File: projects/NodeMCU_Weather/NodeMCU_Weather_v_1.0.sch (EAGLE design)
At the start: 4 parts

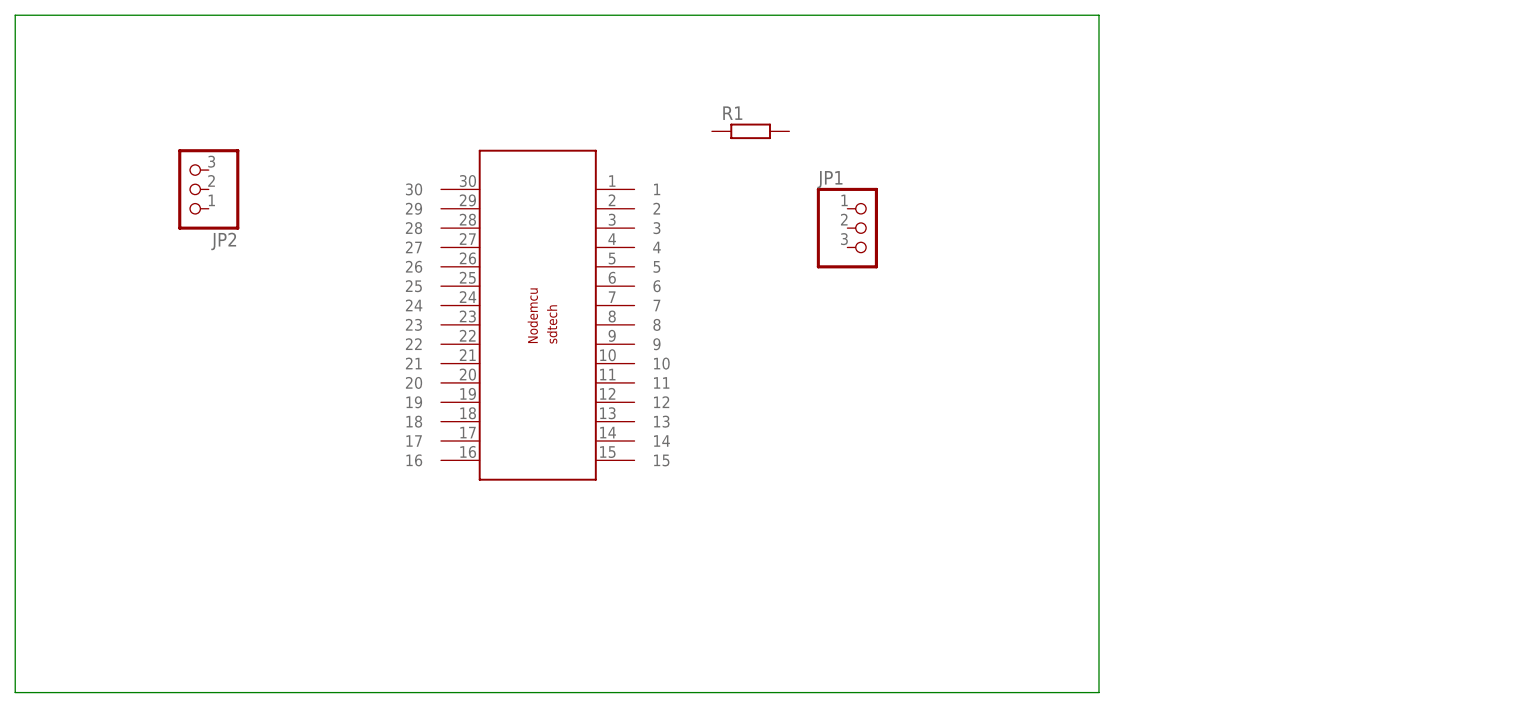
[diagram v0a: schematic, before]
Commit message: Base of nodemcu schematics and board
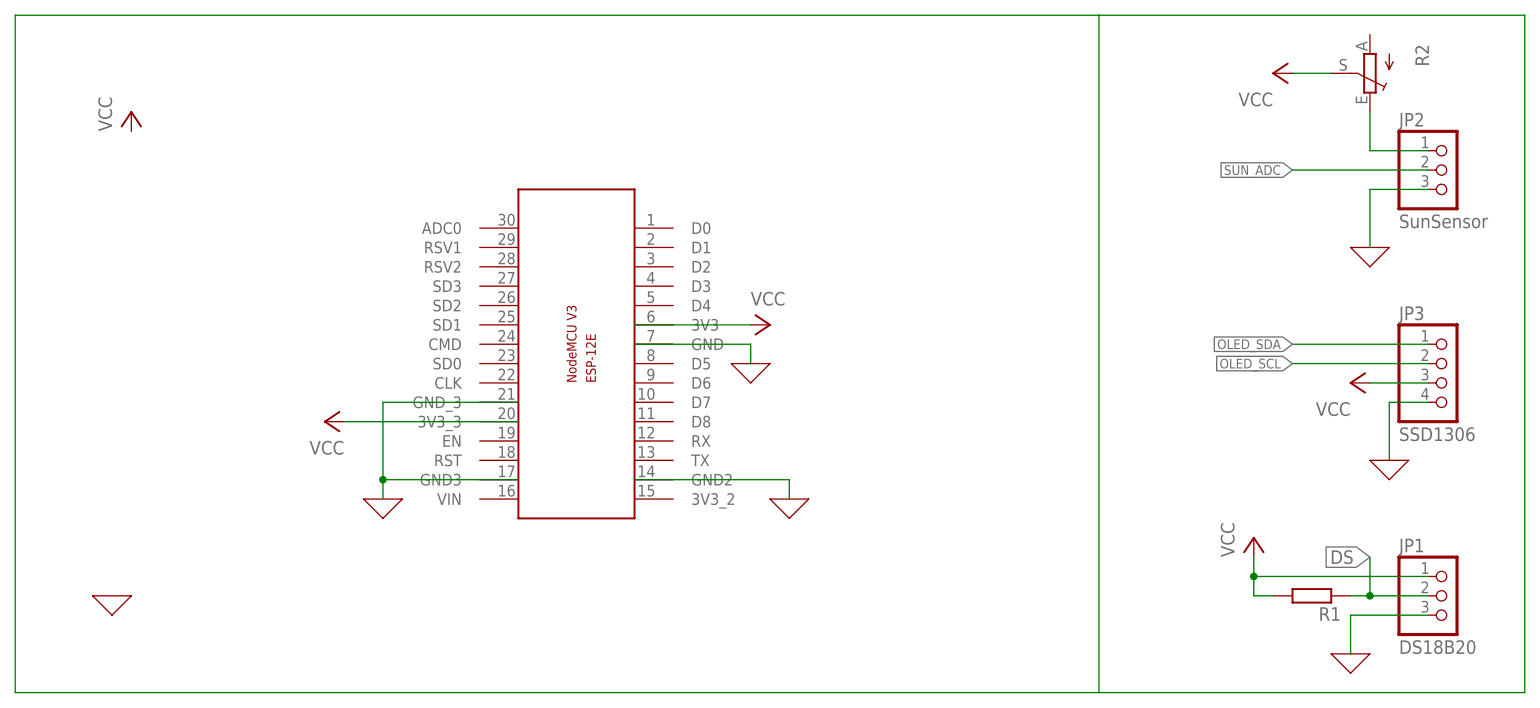
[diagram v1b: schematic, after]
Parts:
- added JP3: SSD1306, pinhead:PINHD-1X4
- added R2: (no value), pot:TRIM_EU-B25P
- JP1: value (none) -> DS18B20
- JP2: value (none) -> SunSensor
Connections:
- new net 0: JP1.3, JP2.3, JP3.4, U$1.GND, U$1.GND2, U$1.GND3, U$1.GND_3
- new net DS: JP1.2, R1.1
- new net N$2: JP2.1, R2.E
- new net OLED_SCL: JP3.2
- new net OLED_SDA: JP3.1
- new net SUN_ADC: JP2.2
- new net VCC: JP1.1, JP3.3, R1.2, R2.S, U$1.3V3, U$1.3V3_3
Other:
- moved on the sheet: JP1, JP2, R1
